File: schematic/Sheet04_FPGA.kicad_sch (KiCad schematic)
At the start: 6 parts

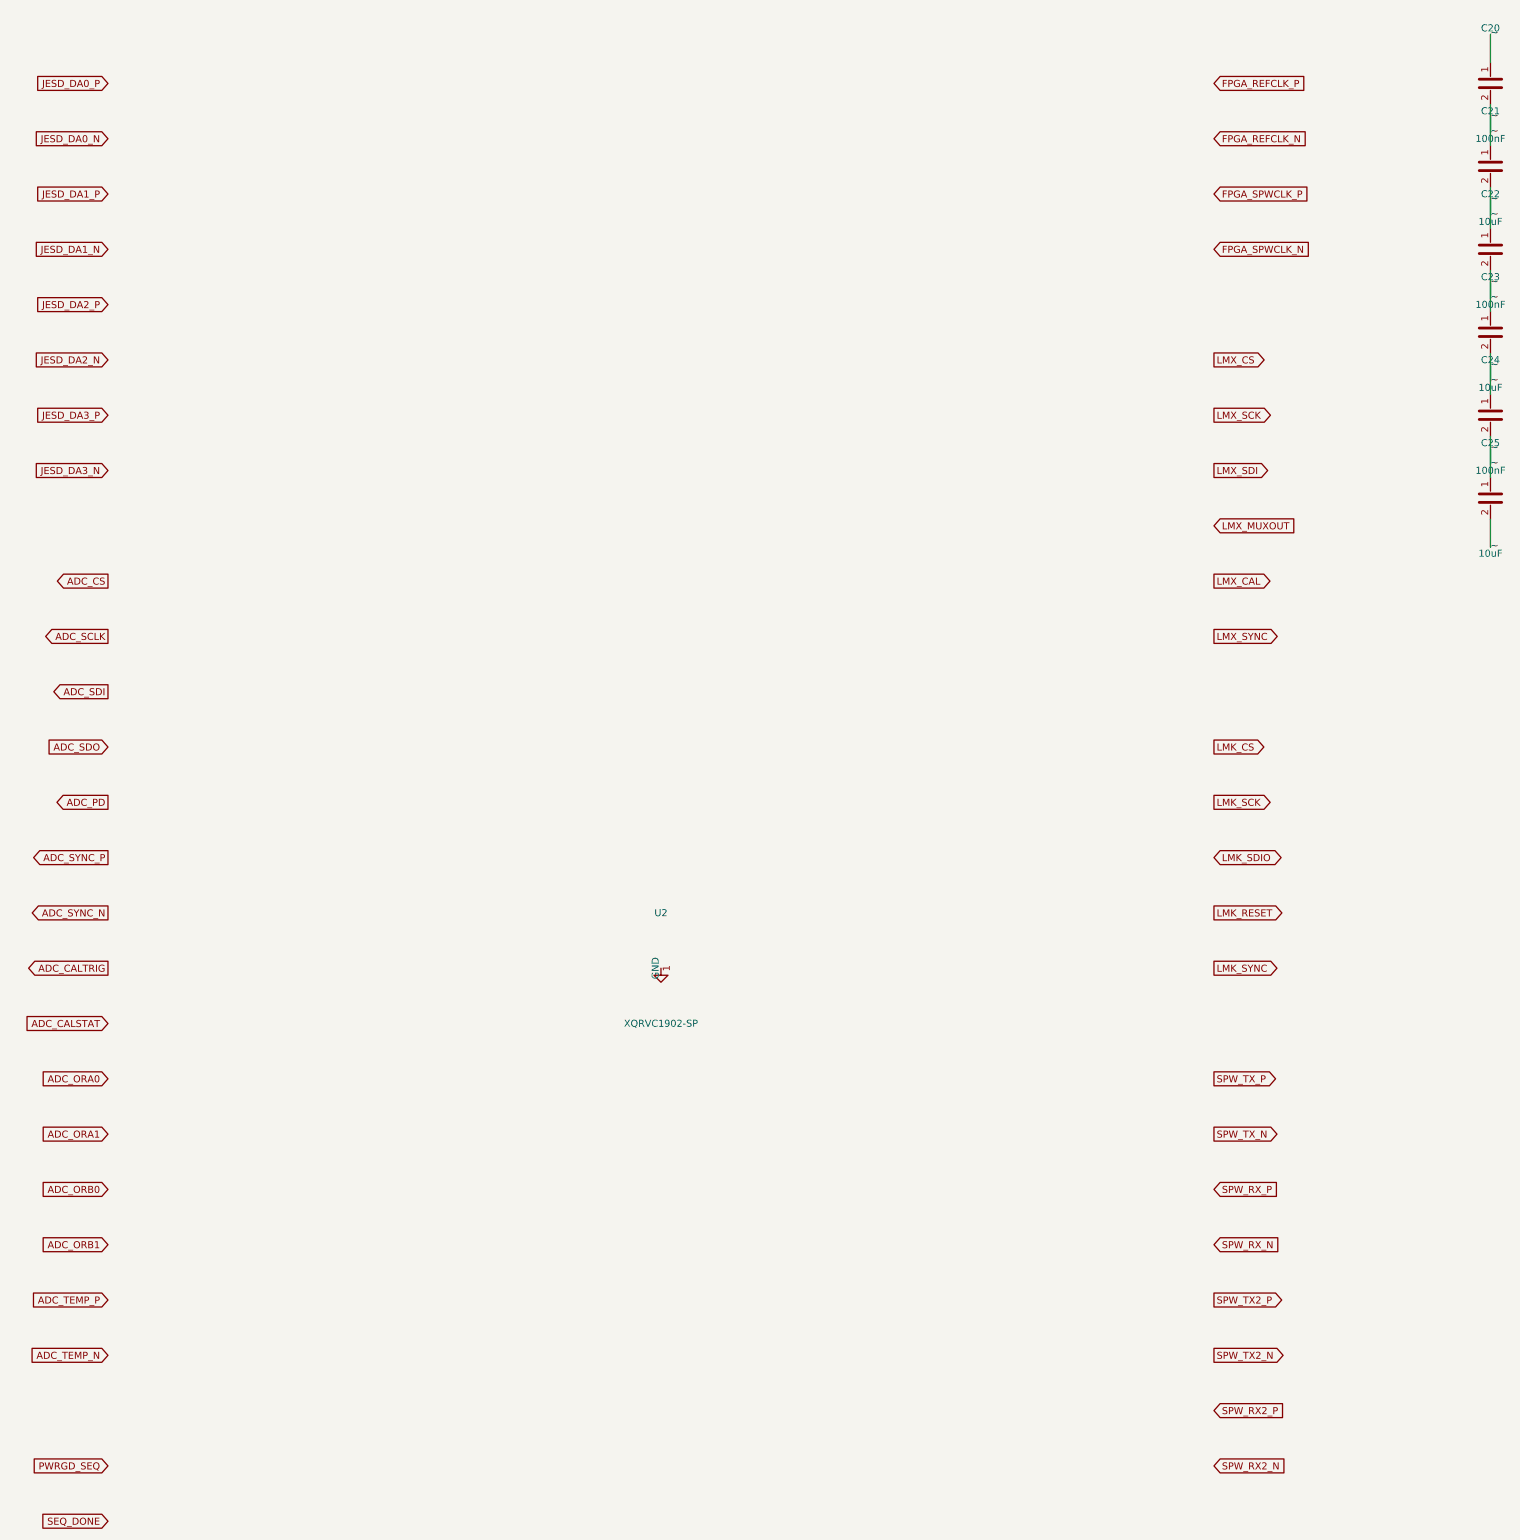
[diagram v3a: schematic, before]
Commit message: Fix KiCad schematic wiring: Y-inversion bug + all 891 pins connected
- Fixed critical Y-axis inversion bug: KiCad inverts Y when placing
  symbols (lib Y + schematic Y = abs Y is WRONG; correct: abs Y = sym Y - lib Y)
- This caused ALL wires to connect to wrong pins (e.g., CS label connected
  to BG pin instead of CS pin)
- Verified with netlist: 0 unconnected nets, all pin functions correct
- Fixed wire direction for angle 90/270 (swapped due to Y-inversion)
- 891 pin connections across 15 sheets, all 17 sheets export without errors
- Netlist verification: CS→E8, BG→C3, INA+→A4, CLK+→F1, JESD pairs correct

Co-Authored-By: opencode <noreply@opencode.ai>
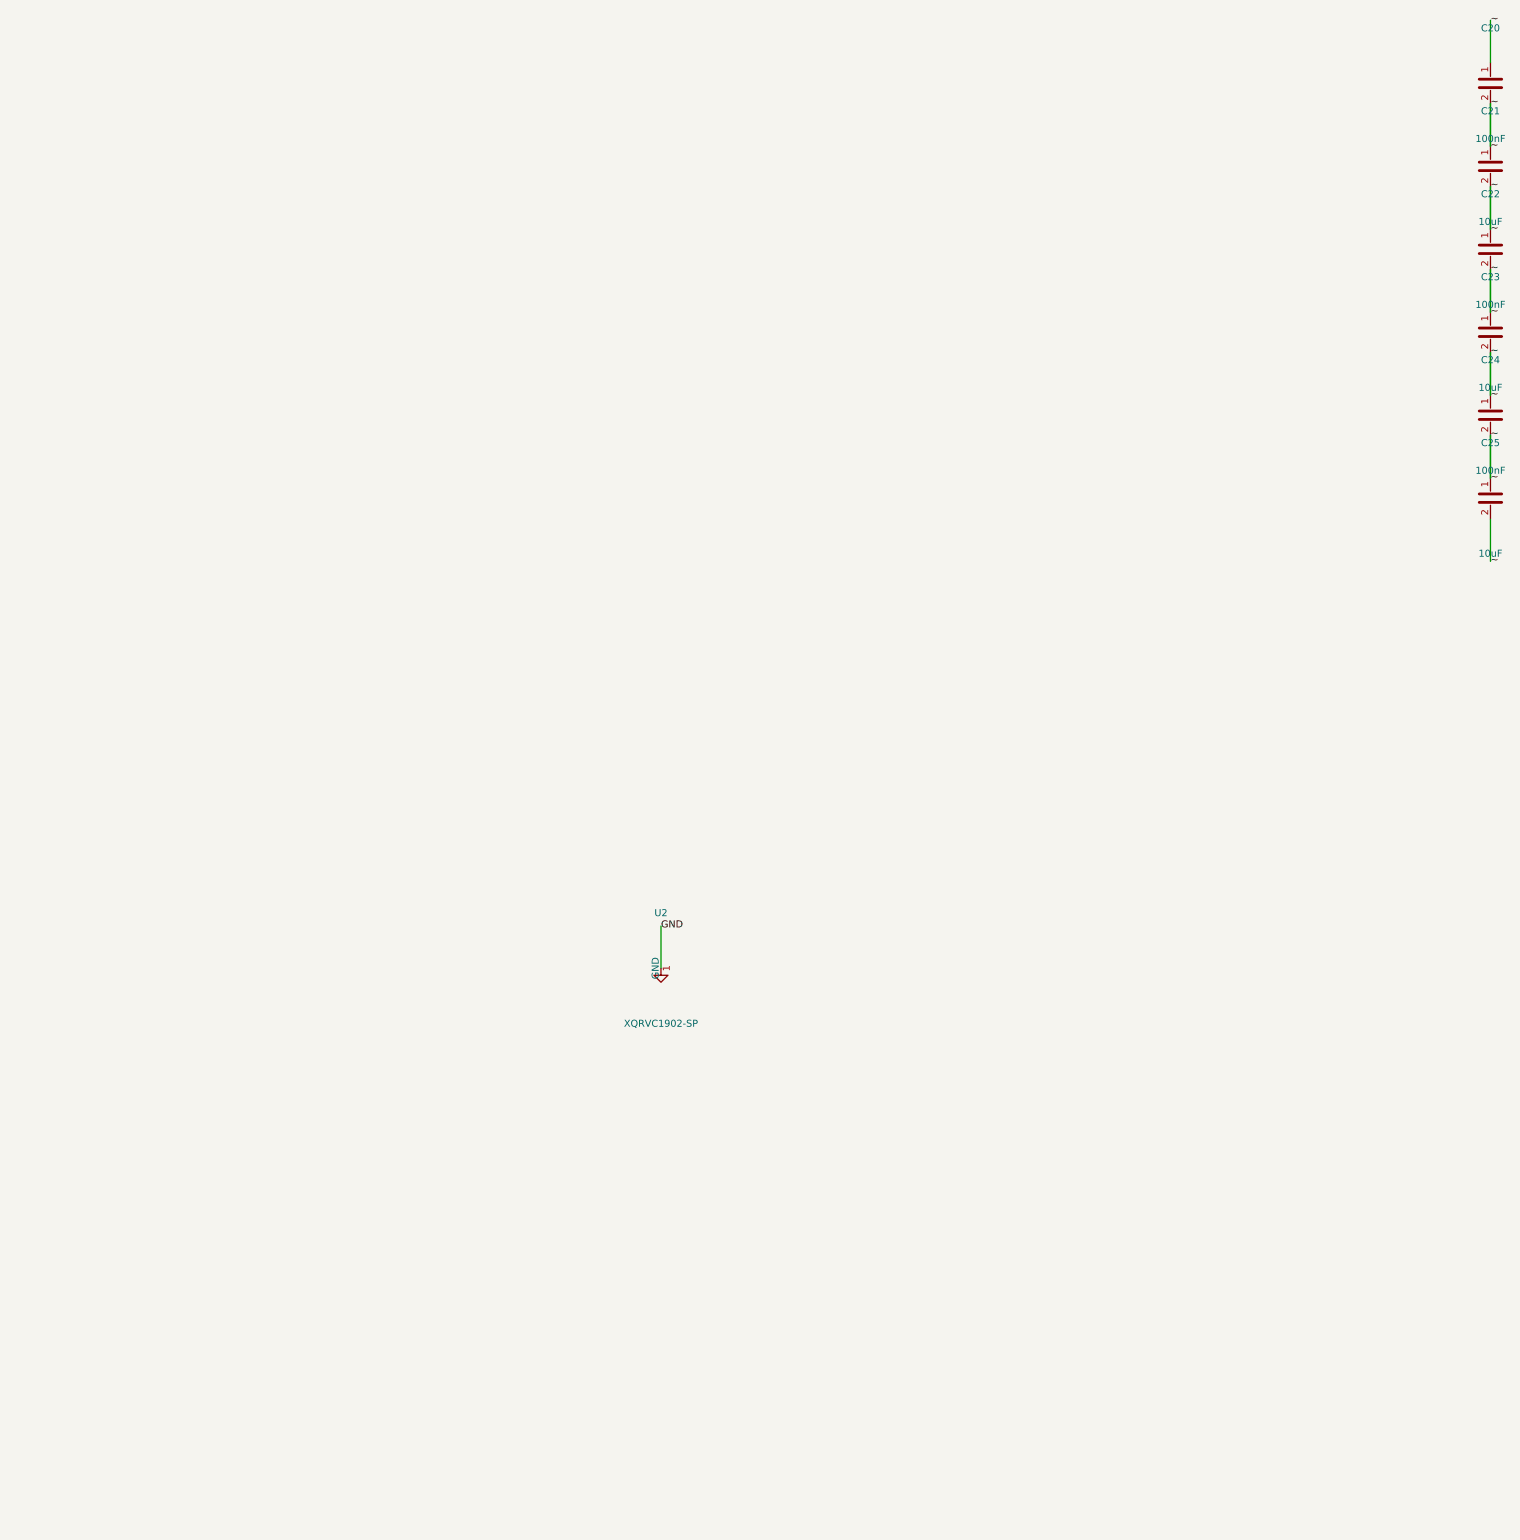
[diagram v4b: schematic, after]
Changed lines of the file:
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@@
     (property "Footprint" "" (at 200 200 0) (effects (font (size 1.27 1.27)) hide))
   )
-  (global_label "JESD_DA0_P" (shape input) (at 100 40 180) (effects (font (size 1.27 1.27)) (justify right)))  (global_label "JESD_DA0_N" (shape input) (at 100 50 180) (effects (font (size 1.27 1.27)) (justify right)))  (global_label "JESD_DA1_P" (shape input) (at 100 60 180) (effects (font (size 1.27 1.27)) (justify right)))  (global_label "JESD_DA1_N" (shape input) (at 100 70 180) (effects (font (size 1.27 1.27)) (justify right)))  (global_label "JESD_DA2_P" (shape input) (at 100 80 180) (effects (font (size 1.27 1.27)) (justify right)))  (global_label "JESD_DA2_N" (shape input) (at 100 90 180) (effects (font (size 1.27 1.27)) (justify right)))  (global_label "JESD_DA3_P" (shape input) (at 100 100 180) (effects (font (size 1.27 1.27)) (justify right)))  (global_label "JESD_DA3_N" (shape input) (at 100 110 180) (effects (font (size 1.27 1.27)) (justify right)))  (global_label "ADC_CS" (shape output) (at 100 130 180) (effects (font (size 1.27 1.27)) (justify right)))  (global_label "ADC_SCLK" (shape output) (at 100 140 180) (effects (font (size 1.27 1.27)) (justify right)))  (global_label "ADC_SDI" (shape output) (at 100 150 180) (effects (font (size 1.27 1.27)) (justify right)))  (global_label "ADC_SDO" (shape input) (at 100 160 180) (effects (font (size 1.27 1.27)) (justify right)))  (global_label "ADC_PD" (shape output) (at 100 170 180) (effects (font (size 1.27 1.27)) (justify right)))  (global_label "ADC_SYNC_P" (shape output) (at 100 180 180) (effects (font (size 1.27 1.27)) (justify right)))  (global_label "ADC_SYNC_N" (shape output) (at 100 190 180) (effects (font (size 1.27 1.27)) (justify right)))  (global_label "ADC_CALTRIG" (shape output) (at 100 200 180) (effects (font (size 1.27 1.27)) (justify right)))  (global_label "ADC_CALSTAT" (shape input) (at 100 210 180) (effects (font (size 1.27 1.27)) (justify right)))  (global_label "ADC_ORA0" (shape input) (at 100 220 180) (effects (font (size 1.27 1.27)) (justify right)))  (global_label "ADC_ORA1" (shape input) (at 100 230 180) (effects (font (size 1.27 1.27)) (justify right)))  (global_label "ADC_ORB0" (shape input) (at 100 240 180) (effects (font (size 1.27 1.27)) (justify right)))  (global_label "ADC_ORB1" (shape input) (at 100 250 180) (effects (font (size 1.27 1.27)) (justify right)))  (global_label "ADC_TEMP_P" (shape input) (at 100 260 180) (effects (font (size 1.27 1.27)) (justify right)))  (global_label "ADC_TEMP_N" (shape input) (at 100 270 180) (effects (font (size 1.27 1.27)) (justify right)))  (global_label "FPGA_REFCLK_P" (shape input) (at 300 40 0) (effects (font (size 1.27 1.27)) (justify left)))  (global_label "FPGA_REFCLK_N" (shape input) (at 300 50 0) (effects (font (size 1.27 1.27)) (justify left)))  (global_label "FPGA_SPWCLK_P" (shape input) (at 300 60 0) (effects (font (size 1.27 1.27)) (justify left)))  (global_label "FPGA_SPWCLK_N" (shape input) (at 300 70 0) (effects (font (size 1.27 1.27)) (justify left)))  (global_label "LMX_CS" (shape output) (at 300 90 0) (effects (font (size 1.27 1.27)) (justify left)))  (global_label "LMX_SCK" (shape output) (at 300 100 0) (effects (font (size 1.27 1.27)) (justify left)))  (global_label "LMX_SDI" (shape output) (at 300 110 0) (effects (font (size 1.27 1.27)) (justify left)))  (global_label "LMX_MUXOUT" (shape input) (at 300 120 0) (effects (font (size 1.27 1.27)) (justify left)))  (global_label "LMX_CAL" (shape output) (at 300 130 0) (effects (font (size 1.27 1.27)) (justify left)))  (global_label "LMX_SYNC" (shape output) (at 300 140 0) (effects (font (size 1.27 1.27)) (justify left)))  (global_label "LMK_CS" (shape output) (at 300 160 0) (effects (font (size 1.27 1.27)) (justify left)))  (global_label "LMK_SCK" (shape output) (at 300 170 0) (effects (font (size 1.27 1.27)) (justify left)))  (global_label "LMK_SDIO" (shape bidirectional) (at 300 180 0) (effects (font (size 1.27 1.27)) (justify left)))  (global_label "LMK_RESET" (shape output) (at 300 190 0) (effects (font (size 1.27 1.27)) (justify left)))  (global_label "LMK_SYNC" (shape output) (at 300 200 0) (effects (font (size 1.27 1.27)) (justify left)))  (global_label "SPW_TX_P" (shape output) (at 300 220 0) (effects (font (size 1.27 1.27)) (justify left)))  (global_label "SPW_TX_N" (shape output) (at 300 230 0) (effects (font (size 1.27 1.27)) (justify left)))  (global_label "SPW_RX_P" (shape input) (at 300 240 0) (effects (font (size 1.27 1.27)) (justify left)))  (global_label "SPW_RX_N" (shape input) (at 300 250 0) (effects (font (size 1.27 1.27)) (justify left)))  (global_label "SPW_TX2_P" (shape output) (at 300 260 0) (effects (font (size 1.27 1.27)) (justify left)))  (global_label "SPW_TX2_N" (shape output) (at 300 270 0) (effects (font (size 1.27 1.27)) (justify left)))  (global_label "SPW_RX2_P" (shape input) (at 300 280 0) (effects (font (size 1.27 1.27)) (justify left)))  (global_label "SPW_RX2_N" (shape input) (at 300 290 0) (effects (font (size 1.27 1.27)) (justify left)))  (global_label "PWRGD_SEQ" (shape input) (at 100 290 180) (effects (font (size 1.27 1.27)) (justify right)))  (global_label "SEQ_DONE" (shape input) (at 100 300 180) (effects (font (size 1.27 1.27)) (justify right)))  (symbol (lib_id "Device:C") (at 350 40 0) (unit 1)
+                                                                                                  (symbol (lib_id "Device:C") (at 350 40 0) (unit 1)
     (in_bom yes) (on_board yes)
     (property "Reference" "C20" (at 350 30 0) (effects (font (size 1.27 1.27))))
@@
     (pin "2")
   )
-  (wire (pts (xy 350.00 43.81) (xy 350.00 48.89)) (stroke (width 0) (type default)))
-  (label "~" (at 350.00 48.89 0) (effects (font (size 1.27 1.27))))
-  (wire (pts (xy 350.00 36.19) (xy 350.00 31.11)) (stroke (width 0) (type default)))
-  (label "~" (at 350.00 31.11 0) (effects (font (size 1.27 1.27))))
-  (wire (pts (xy 350.00 58.81) (xy 350.00 63.89)) (stroke (width 0) (type default)))
-  (label "~" (at 350.00 63.89 0) (effects (font (size 1.27 1.27))))
-  (wire (pts (xy 350.00 51.19) (xy 350.00 46.11)) (stroke (width 0) (type default)))
-  (label "~" (at 350.00 46.11 0) (effects (font (size 1.27 1.27))))
-  (wire (pts (xy 350.00 73.81) (xy 350.00 78.89)) (stroke (width 0) (type default)))
-  (label "~" (at 350.00 78.89 0) (effects (font (size 1.27 1.27))))
-  (wire (pts (xy 350.00 66.19) (xy 350.00 61.11)) (stroke (width 0) (type default)))
-  (label "~" (at 350.00 61.11 0) (effects (font (size 1.27 1.27))))
-  (wire (pts (xy 350.00 88.81) (xy 350.00 93.89)) (stroke (width 0) (type default)))
-  (label "~" (at 350.00 93.89 0) (effects (font (size 1.27 1.27))))
-  (wire (pts (xy 350.00 81.19) (xy 350.00 76.11)) (stroke (width 0) (type default)))
-  (label "~" (at 350.00 76.11 0) (effects (font (size 1.27 1.27))))
-  (wire (pts (xy 350.00 103.81) (xy 350.00 108.89)) (stroke (width 0) (type default)))
-  (label "~" (at 350.00 108.89 0) (effects (font (size 1.27 1.27))))
-  (wire (pts (xy 350.00 96.19) (xy 350.00 91.11)) (stroke (width 0) (type default)))
-  (label "~" (at 350.00 91.11 0) (effects (font (size 1.27 1.27))))
-  (wire (pts (xy 350.00 118.81) (xy 350.00 123.89)) (stroke (width 0) (type default)))
-  (label "~" (at 350.00 123.89 0) (effects (font (size 1.27 1.27))))
-  (wire (pts (xy 350.00 111.19) (xy 350.00 106.11)) (stroke (width 0) (type default)))
-  (label "~" (at 350.00 106.11 0) (effects (font (size 1.27 1.27))))
+  (wire (pts (xy 200.0000 200.0000) (xy 200.0000 192.3800)) (stroke (width 0) (type default)))
+  (label "GND" (at 200.0000 192.3800 0) (effects (font (size 1.27 1.27))))
+  (wire (pts (xy 350.0000 36.1900) (xy 350.0000 28.5700)) (stroke (width 0) (type default)))
+  (label "~" (at 350.0000 28.5700 0) (effects (font (size 1.27 1.27))))
+  (wire (pts (xy 350.0000 43.8100) (xy 350.0000 51.4300)) (stroke (width 0) (type default)))
+  (label "~" (at 350.0000 51.4300 0) (effects (font (size 1.27 1.27))))
+  (wire (pts (xy 350.0000 51.1900) (xy 350.0000 43.5700)) (stroke (width 0) (type default)))
+  (label "~" (at 350.0000 43.5700 0) (effects (font (size 1.27 1.27))))
+  (wire (pts (xy 350.0000 58.8100) (xy 350.0000 66.4300)) (stroke (width 0) (type default)))
+  (label "~" (at 350.0000 66.4300 0) (effects (font (size 1.27 1.27))))
+  (wire (pts (xy 350.0000 66.1900) (xy 350.0000 58.5700)) (stroke (width 0) (type default)))
+  (label "~" (at 350.0000 58.5700 0) (effects (font (size 1.27 1.27))))
+  (wire (pts (xy 350.0000 73.8100) (xy 350.0000 81.4300)) (stroke (width 0) (type default)))
+  (label "~" (at 350.0000 81.4300 0) (effects (font (size 1.27 1.27))))
+  (wire (pts (xy 350.0000 81.1900) (xy 350.0000 73.5700)) (stroke (width 0) (type default)))
+  (label "~" (at 350.0000 73.5700 0) (effects (font (size 1.27 1.27))))
+  (wire (pts (xy 350.0000 88.8100) (xy 350.0000 96.4300)) (stroke (width 0) (type default)))
+  (label "~" (at 350.0000 96.4300 0) (effects (font (size 1.27 1.27))))
+  (wire (pts (xy 350.0000 96.1900) (xy 350.0000 88.5700)) (stroke (width 0) (type default)))
+  (label "~" (at 350.0000 88.5700 0) (effects (font (size 1.27 1.27))))
+  (wire (pts (xy 350.0000 103.8100) (xy 350.0000 111.4300)) (stroke (width 0) (type default)))
+  (label "~" (at 350.0000 111.4300 0) (effects (font (size 1.27 1.27))))
+  (wire (pts (xy 350.0000 111.1900) (xy 350.0000 103.5700)) (stroke (width 0) (type default)))
+  (label "~" (at 350.0000 103.5700 0) (effects (font (size 1.27 1.27))))
+  (wire (pts (xy 350.0000 118.8100) (xy 350.0000 126.4300)) (stroke (width 0) (type default)))
+  (label "~" (at 350.0000 126.4300 0) (effects (font (size 1.27 1.27))))
   (sheet_instances (path "/" (page "1")))
 )
